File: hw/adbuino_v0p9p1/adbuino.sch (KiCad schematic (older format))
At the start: 68 parts, among them IC1 MAX3421EEHJ+, J1 Conn_01x06_Male, J2 U254-051N-4BH806, J3 USB_A, J4 Mini-DIN-4, J5 Mini-DIN-4, U1 AMS1117-3.3, U2 ATmega328P-AU, Y1 16MHz, Y2 12MHz

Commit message: updates
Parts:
- removed TP10, TP9: TestPoint_Small, TestPoint:TestPoint_Pad_D1.0mm, symbol Connector:TestPoint_Small
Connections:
- net TTL_SPI_MOSI is gone; now on net ATMEGA_SPI_MOSI: TP25.1
- net TTL_SPI_SCLK is gone; now on net ATMEGA_SPI_SCLK: TP22.1
- net ATMEGA_SPI_MISO: now also TP14.1
- net SPI_MISO: no longer TP14.1
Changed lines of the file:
@@
 	0    -1   -1   0
 $EndComp
-Text GLabel 5500 4500 0    50   Input ~ 0
-SPI_MISO
-Text GLabel 6000 4600 2    50   Input ~ 0
-TTL_SPI_MOSI
-Text GLabel 5500 4600 0    50   Input ~ 0
-TTL_SPI_SCLK
 NoConn ~ 4850 1200
 NoConn ~ 2250 5400
@@
 $EndComp
 $Comp
-L Connector:TestPoint_Small TP10
-U 1 1 610DB1F2
-P 2350 6200
-F 0 "TP10" H 2350 6250 50  0000 L CNN
-F 1 "TestPoint_Small" H 2398 6155 50  0001 L CNN
-F 2 "TestPoint:TestPoint_Pad_D1.0mm" H 2550 6200 50  0001 C CNN
-F 3 "~" H 2550 6200 50  0001 C CNN
-	1    2350 6200
-	1    0    0    -1
-$EndComp
-$Comp
-L Connector:TestPoint_Small TP9
-U 1 1 610DB1F8
-P 2350 6100
-F 0 "TP9" H 2350 6150 50  0000 L CNN
-F 1 "TestPoint_Small" H 2398 6055 50  0001 L CNN
-F 2 "TestPoint:TestPoint_Pad_D1.0mm" H 2550 6100 50  0001 C CNN
-F 3 "~" H 2550 6100 50  0001 C CNN
-	1    2350 6100
-	1    0    0    -1
-$EndComp
-$Comp
 L Connector:TestPoint_Small TP13
 U 1 1 610DB204
@@
 Wire Wire Line
 	2350 6300 2500 6300
-Wire Wire Line
-	2250 6200 2350 6200
-Connection ~ 2350 6200
-Wire Wire Line
-	2350 6200 2500 6200
-Wire Wire Line
-	2250 6100 2350 6100
-Connection ~ 2350 6100
-Wire Wire Line
-	2350 6100 2500 6100
 Wire Wire Line
 	2250 6800 2350 6800
@@
 $EndComp
 $Comp
-L power:GND #PWR?
+L power:GND #PWR0102
 U 1 1 614ED05B
 P 10300 1000
-F 0 "#PWR?" H 10300 750 50  0001 C CNN
+F 0 "#PWR0102" H 10300 750 50  0001 C CNN
 F 1 "GND" V 10300 850 50  0000 R CNN
 F 2 "" H 10300 1000 50  0001 C CNN
@@
 $EndComp
 $Comp
-L power:GND #PWR?
+L power:GND #PWR0103
 U 1 1 614F679B
 P 10300 2000
-F 0 "#PWR?" H 10300 1750 50  0001 C CNN
+F 0 "#PWR0103" H 10300 1750 50  0001 C CNN
 F 1 "GND" V 10300 1850 50  0000 R CNN
 F 2 "" H 10300 2000 50  0001 C CNN
@@
 	0    1    1    0
 $EndComp
+Wire Wire Line
+	2250 6200 2500 6200
+Wire Wire Line
+	2500 6100 2250 6100
+Text GLabel 5500 4500 0    50   Input ~ 0
+ATMEGA_SPI_MISO
+Text GLabel 6000 4600 2    50   Input ~ 0
+ATMEGA_SPI_MOSI
+Text GLabel 5500 4600 0    50   Input ~ 0
+ATMEGA_SPI_SCLK
 $EndSCHEMATC

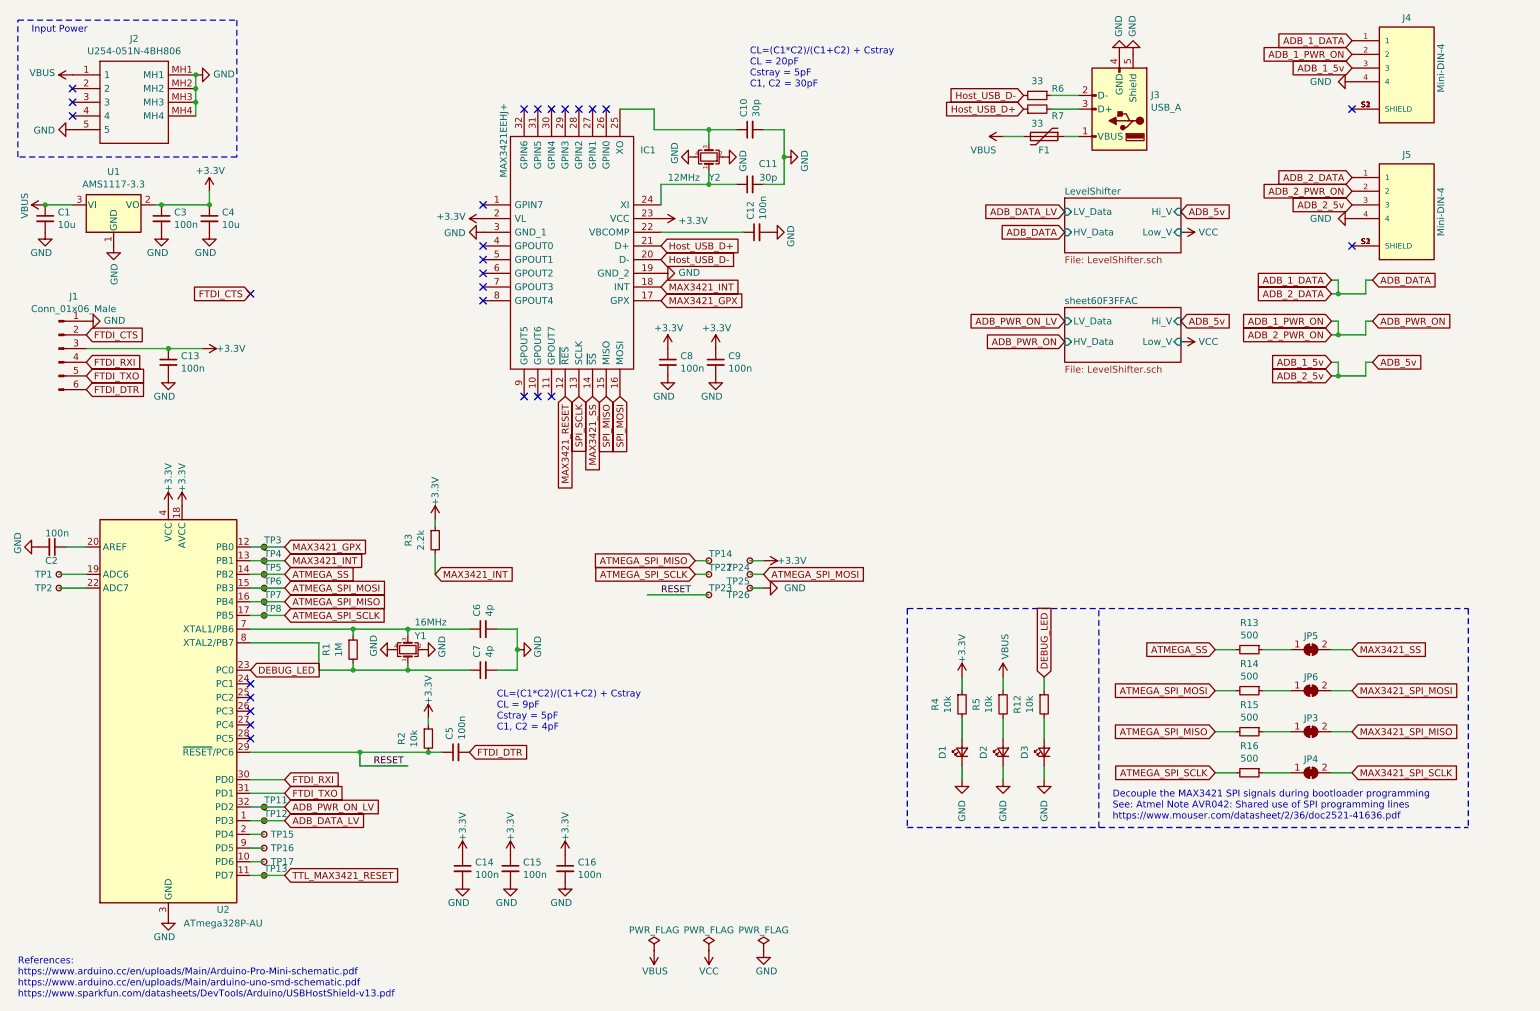
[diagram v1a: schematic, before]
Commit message: First round of routing completed
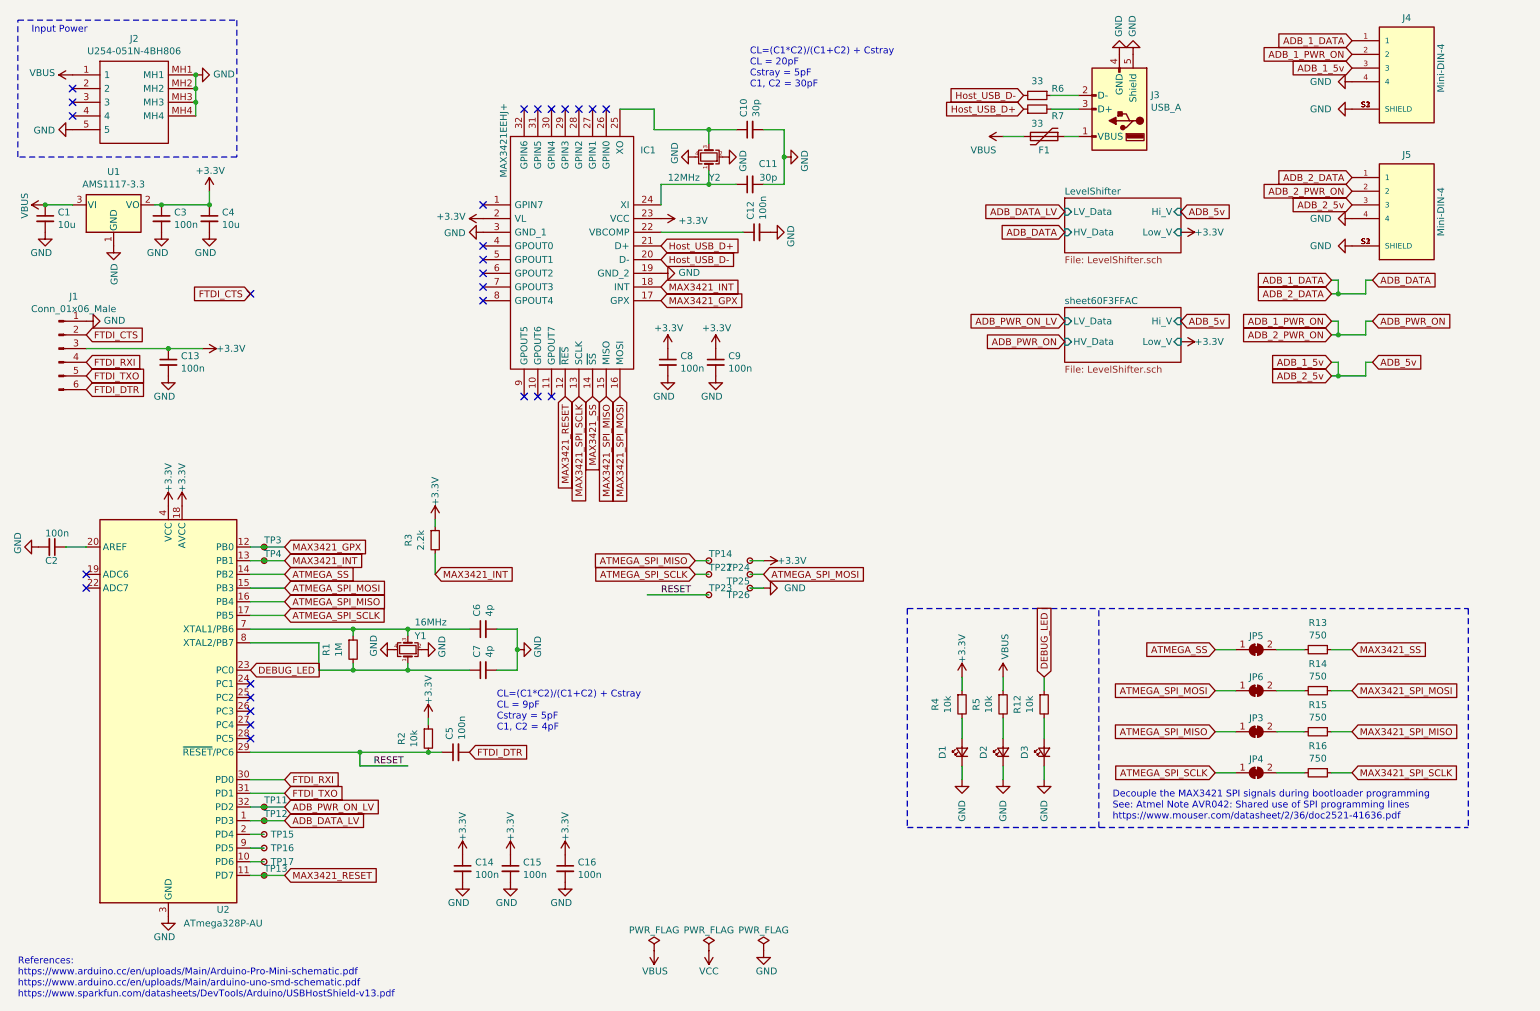
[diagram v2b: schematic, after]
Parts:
- removed TP1, TP2, TP5, TP6, TP7, TP8: TestPoint_Small, TestPoint:TestPoint_Pad_D1.0mm, symbol Connector:TestPoint_Small
- C1, C4: LCSC C15850 -> C15525
- C10, C11: LCSC C1809 -> C1570
- C12, C13, C14, C15, C16, C2, C3, C5, C8, C9: LCSC C49678 -> C1525
- C6, C7: LCSC C170115 -> C318615
- R1: LCSC C17514 -> C26083
- R12, R2, R4, R5: LCSC C17414 -> C25744
- R13, R14, R15, R16: value 500 -> 750; LCSC (none) -> C445595
- R3: LCSC C17520 -> C25879
- R6, R7: LCSC C17634 -> C25105
- U2: LCSC (none) -> C14877
- Y2: footprint Crystal:Crystal_SMD_5032-4Pin_5.0x3.2mm -> Crystal:Crystal_SMD_3225-4Pin_3.2x2.5mm
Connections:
- net SPI_MISO is gone; now on net MAX3421_SPI_MISO: IC1.15 (MISO)
- net SPI_MOSI is gone; now on net MAX3421_SPI_MOSI: IC1.16 (MOSI)
- net SPI_SCLK is gone; now on net MAX3421_SPI_SCLK: IC1.13 (SCLK)
- net TTL_MAX3421_RESET is gone; now on net MAX3421_RESET: TP13.1, U2.11 (PD7)
- net ATMEGA_SPI_MISO: now also JP3.1 (A); no longer R15.2
- net ATMEGA_SPI_MOSI: now also JP6.1 (A); no longer R14.2
- net ATMEGA_SPI_SCLK: now also JP4.1 (A); no longer R16.2
- net ATMEGA_SS: now also JP5.1 (A); no longer R13.2
- net GND: now also J4.S1 (SHIELD), J4.S2 (SHIELD), J4.S3 (SHIELD), J5.S1 (SHIELD), J5.S2 (SHIELD), J5.S3 (SHIELD)
- net MAX3421_SPI_MISO: now also R15.1; no longer JP3.2 (B)
- net MAX3421_SPI_MOSI: now also R14.1; no longer JP6.2 (B)
- net MAX3421_SPI_SCLK: now also R16.1; no longer JP4.2 (B)
- net MAX3421_SS: now also R13.1; no longer JP5.2 (B)
- new net: JP3.2 (B), R15.2
- new net: JP4.2 (B), R16.2
- new net: JP5.2 (B), R13.2
- new net: JP6.2 (B), R14.2
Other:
- moved on the sheet: JP3, JP4, JP5, JP6, R13, R14, R15, R16

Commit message: Added 3d models for connectors
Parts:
- J2: LCSC (none) -> C319170
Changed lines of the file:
@@
 F 10 "" H 1700 250 50  0001 L CNN "Mouser Part Number"
 F 11 "" H 1700 150 50  0001 L CNN "Mouser Price/Stock"
+F 12 "C319170" H 950 950 50  0001 C CNN "LCSC"
 	1    950  950
 	1    0    0    -1
